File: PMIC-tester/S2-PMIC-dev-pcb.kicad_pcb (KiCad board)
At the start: 2 copper layers, 99.1 x 50 mm, 21 parts, among them J1 USB_C_Receptacle_USB2.0, P1 CONN_02X13, P3 CONN_02X13, SW1 RESET, SW2 BOOT, U1 MCP1700-1202E_SOT23, U2 ESP32-S2-WROVER, U3 TPS65185RGZR

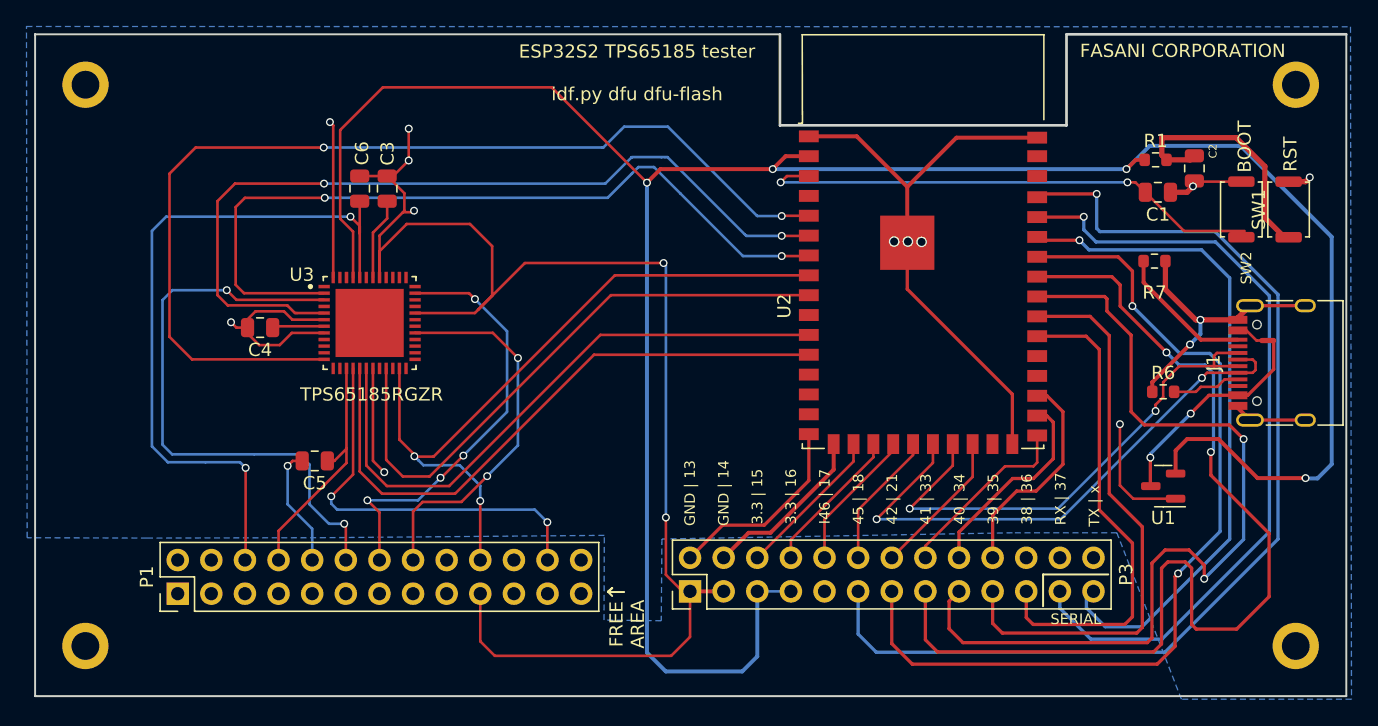
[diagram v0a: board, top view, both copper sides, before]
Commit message: Minimal update with TPs
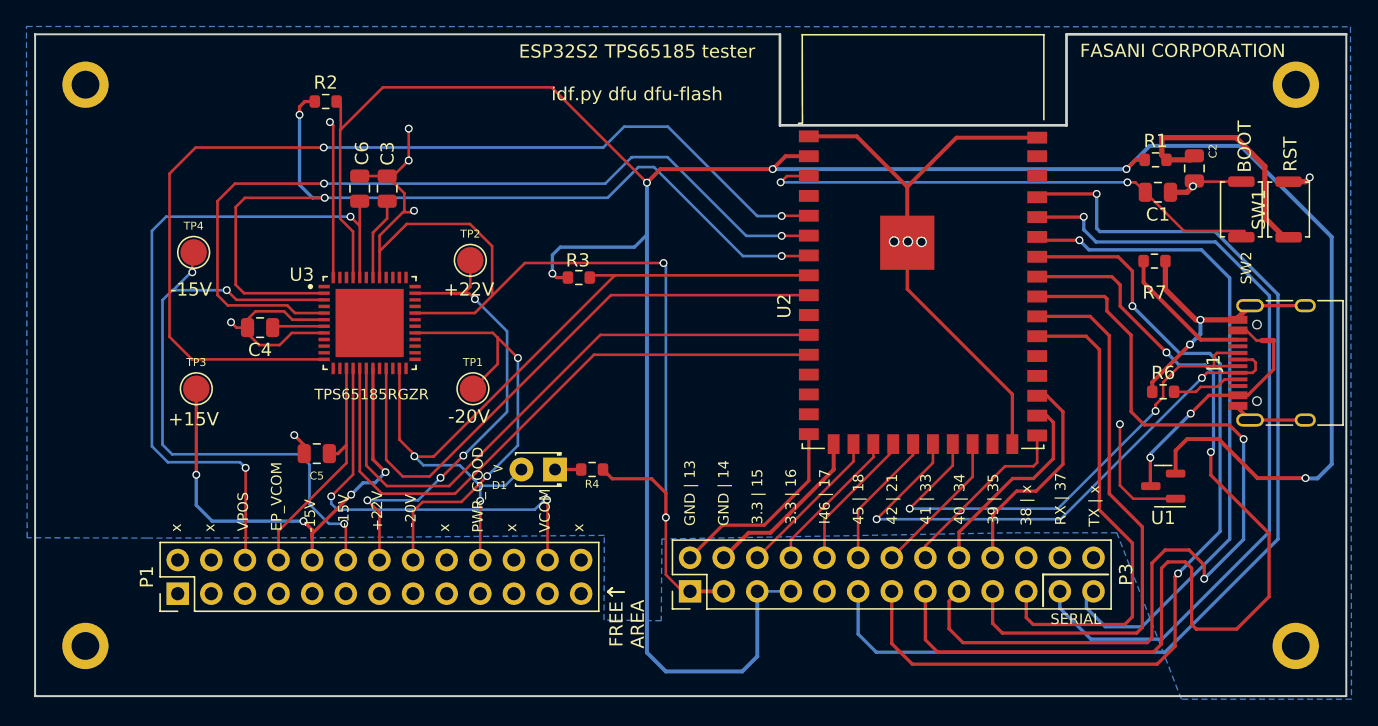
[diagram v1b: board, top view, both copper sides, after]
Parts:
- added D1: LED, LED_THT:LED_D1.8mm_W3.3mm_H2.4mm, F.Cu at (135.8, 104.0)
- added R2: 10k, Resistor_SMD:R_0603_1608Metric, F.Cu at (118.5, 76.2)
- added R3: 10k, Resistor_SMD:R_0603_1608Metric, F.Cu at (137.6, 89.5)
- added R4: 1k, Resistor_SMD:R_0603_1608Metric, F.Cu at (138.6, 104.0)
- added TP1: -20V, TestPoint:TestPoint_Pad_D2.0mm, F.Cu at (129.6, 97.9)
- added TP2: +22V, TestPoint:TestPoint_Pad_D2.0mm, F.Cu at (129.4, 88.2)
- added TP3: +15V, TestPoint:TestPoint_Pad_D2.0mm, F.Cu at (108.7, 97.9)
- added TP4: +15V, TestPoint:TestPoint_Pad_D2.0mm, F.Cu at (108.5, 87.6)
- moved C5 0.57 mm to (117.8, 102.8)
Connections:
- P1 pad 10: GND -> /+15V
- P1 pad 19: GND -> unconnected-(P1-Pad19)
- U3 pad 19: GND -> /+15V
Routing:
- net GND: track 237.3 -> 199.9 mm, vias 17 -> 16
- net /+15V: track 0.00 -> 36.6 mm, vias 0 -> 4
- net /3.3V: track 184.7 -> 197.4 mm, vias 4 -> 5
- net /TPS_INT: track 60.2 -> 69.6 mm, vias 2 -> 3
- net /TPS_PWR_GOOD: track 54.1 -> 59.4 mm
- net /-20V: track 28.8 -> 33.4 mm
- net /+22V: track 32.4 -> 36.0 mm
- net /-15V: track 44.5 -> 48.0 mm, vias 2 -> 3
- net Net-(D1-Pad1): track 0.00 -> 1.97 mm
- net /TPS_VCOM_POWER: track 30.7 -> 32.2 mm
- net /VPOS: track 53.8 -> 53.1 mm
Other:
- board text added: "+15V"
- board text added: "+22V"
- board text added: "-15V"
- board text added: "-20V"
- board text added: "38 | x"
- board text added: ">"
- board text added: "EP_VCOM"
- board text added: "PWR_GOOD"
- board text added: "VCOM"
- board text added: "VPOS"
- board text added: "x"
- board text removed: "38 | 36"
